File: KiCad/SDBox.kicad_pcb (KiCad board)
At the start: 4 copper layers, 52.5 x 59 mm, 20 parts, among them J1 DB25_Male, J2 Micro_SD_Card_Socket, U1 Rapberry_Pi_Pico_2W, U2 SN74CBT16210

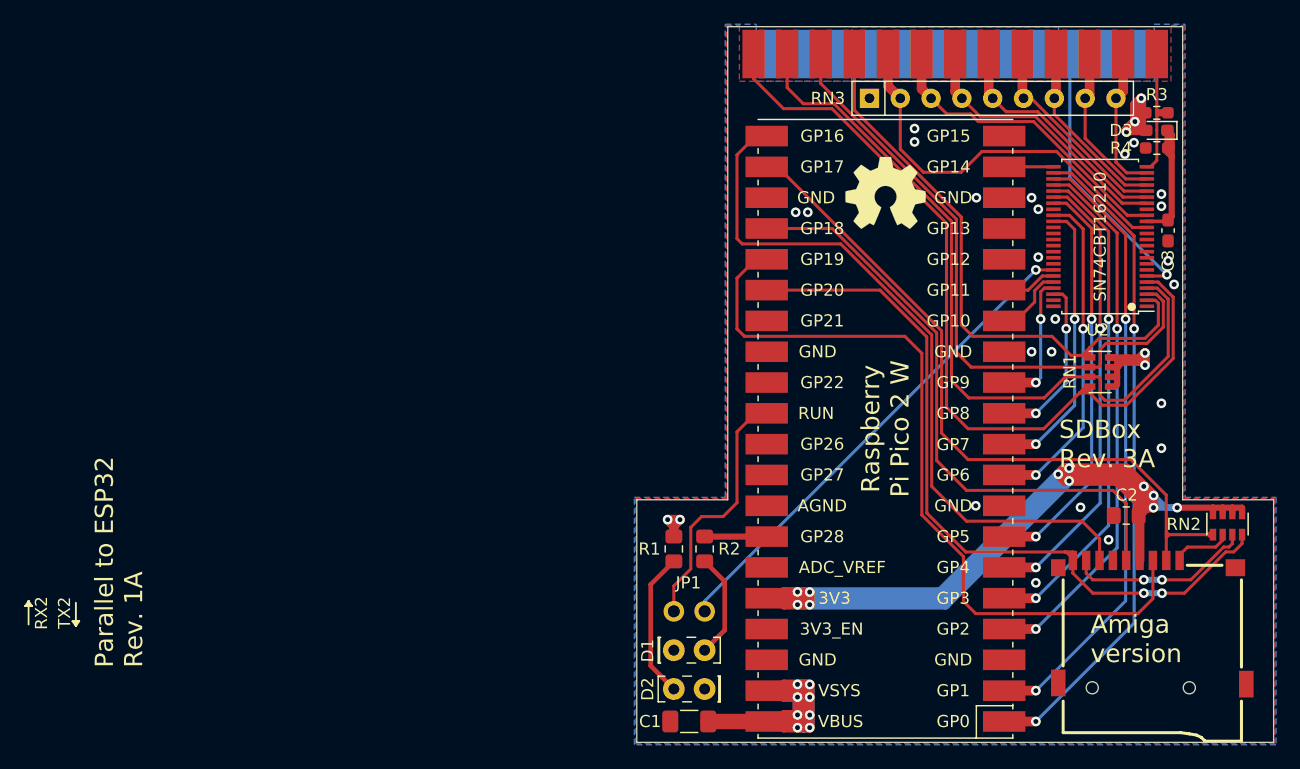
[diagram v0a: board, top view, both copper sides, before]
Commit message: Add UART0_TX and UART0_RX through level shifter
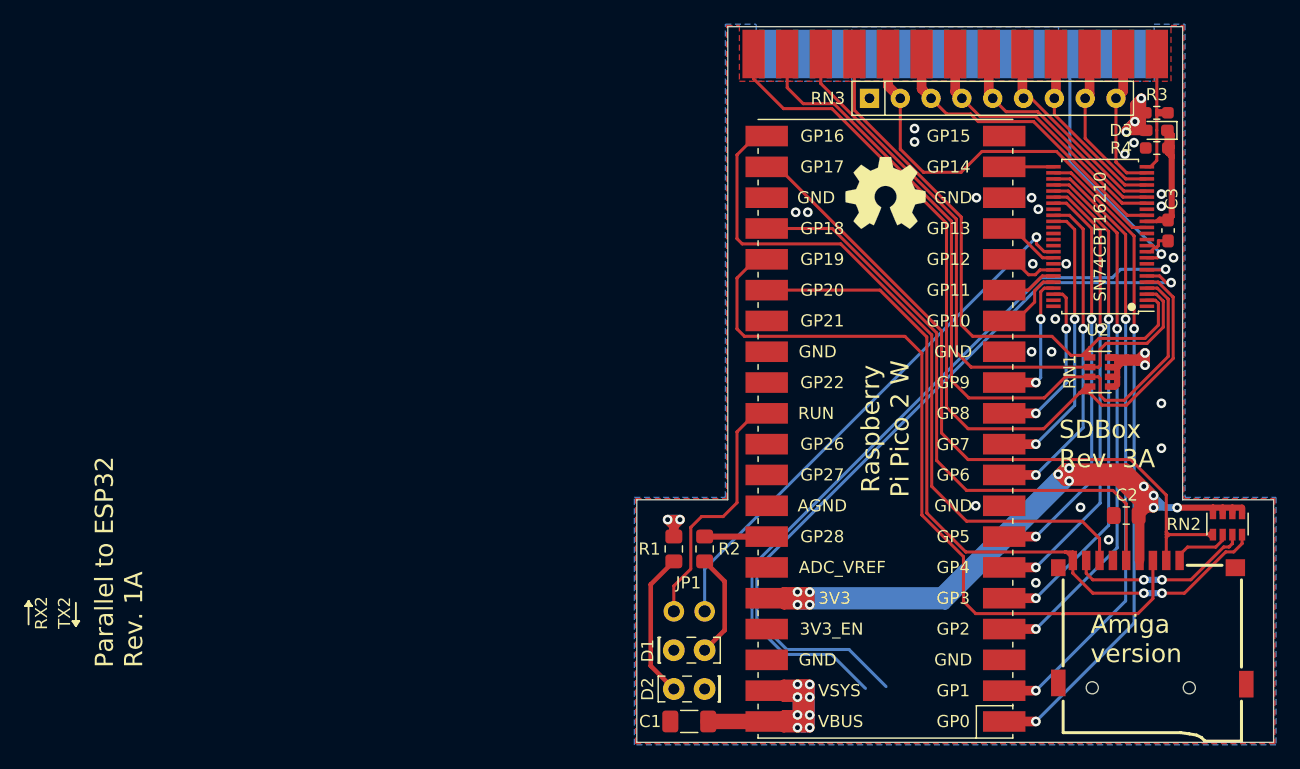
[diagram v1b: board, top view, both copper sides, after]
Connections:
- U1 pad 16: Net-(U1-Pad16) -> UART0_TX_3V3
- U1 pad 17: Net-(U1-Pad17) -> UART0_RX_3V3
- U2 pad 39: Net-(U2-Pad39) -> RESET_3V3
- U2 pad 40: Net-(U2-Pad40) -> UART0_RX_3V3
- U2 pad 42: RESET_3V3 -> UART0_TX_3V3
- U2 pad 6: RESET -> UART0_TX
- U2 pad 7: GND -> UART0_RX
- U2 pad 9: GND -> RESET
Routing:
- net UART0_TX: track 0.00 -> 63.3 mm, vias 0 -> 1
- net UART0_RX: track 0.00 -> 62.0 mm, vias 0 -> 1
- net UART0_RX_3V3: track 0.00 -> 5.96 mm
- net UART0_TX_3V3: track 0.00 -> 5.65 mm
- net RESET_3V3: track 41.0 -> 44.4 mm
- net GND: track 0.00 -> 2.36 mm
- net RESET: track 23.7 -> 21.4 mm
- net VCC: track 75.2 -> 77.2 mm
- net /4V3: track 12.3 -> 13.4 mm

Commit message: Improve ground stitching
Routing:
- net GND: vias 23 -> 33

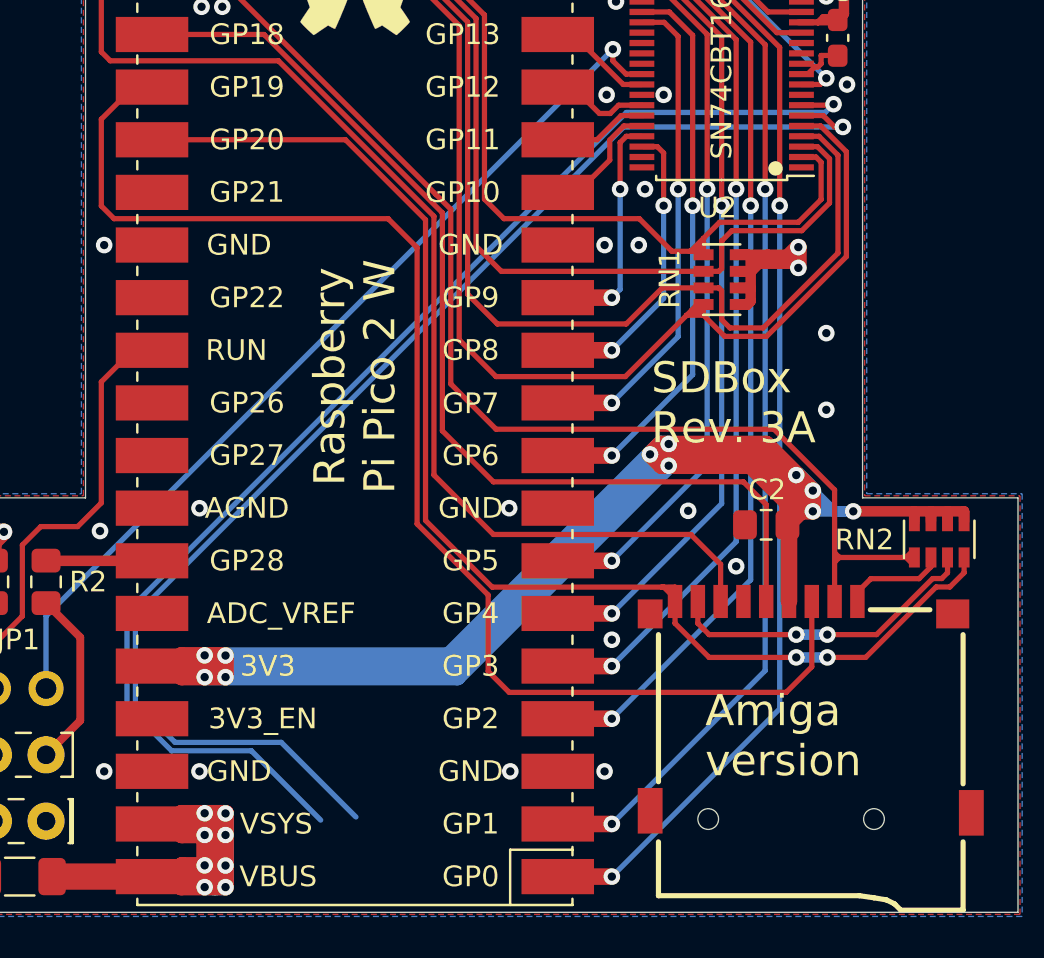
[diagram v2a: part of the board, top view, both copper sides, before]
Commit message: Add UART pinheader on underside with TX0 (GP12), RX0 (GP13) and Power and GND
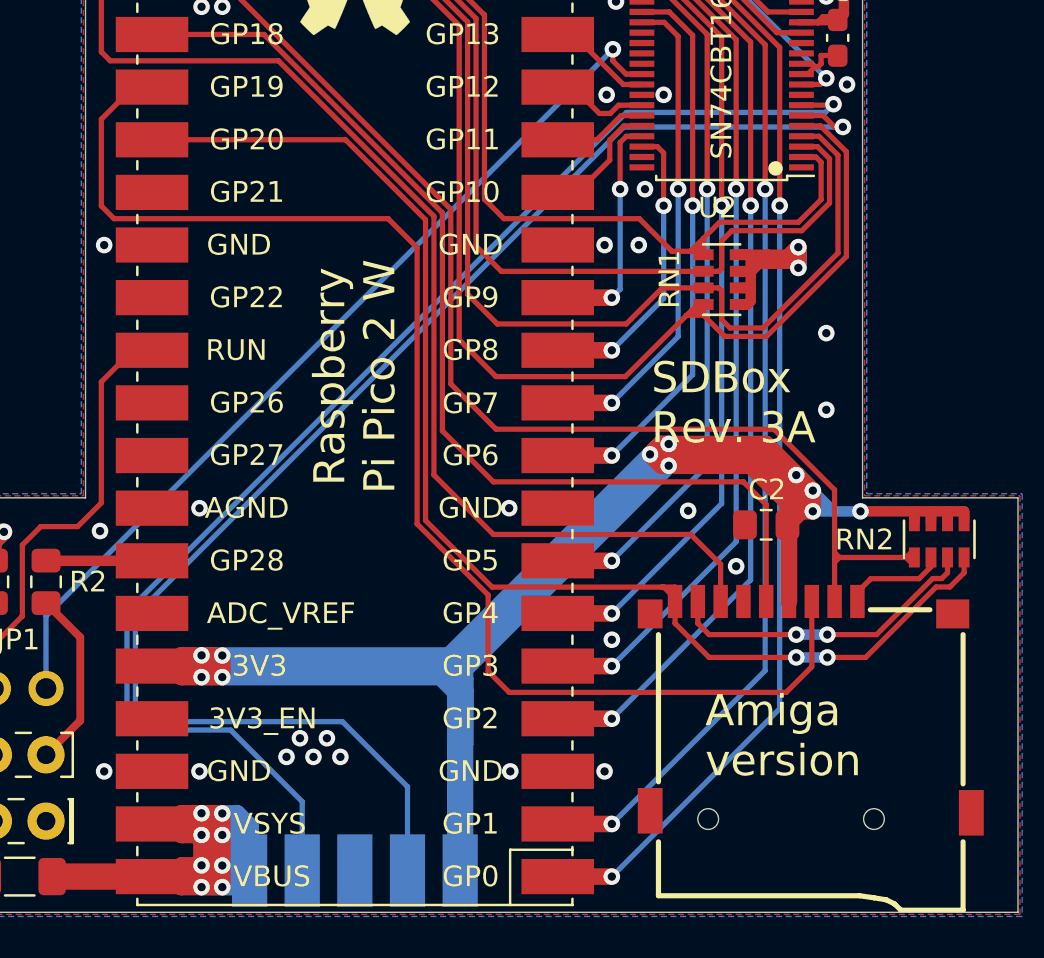
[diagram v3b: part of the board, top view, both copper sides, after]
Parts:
- added J3: Conn_01x05, SDBox:UART_PinHeader_SMD_pads_2.54mm_pitch, B.Cu at (141.9, 142.2)
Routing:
- net 3V3: track 141.7 -> 154.6 mm
- net VCC: track 77.2 -> 88.3 mm
- net UART0_TX: track 63.3 -> 68.3 mm
- net UART0_RX: track 62.0 -> 63.2 mm
- net GND: vias 33 -> 38

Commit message: Improve routing
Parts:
- moved REF** 0.50 mm to (147.7, 113.5)
- moved RN3 0.07 mm to (140.7, 90.9)
- renumbered D2 to D1, D1 to D2
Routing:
- net VCC: track 88.3 -> 86.3 mm
- net CP: track 61.6 -> 60.7 mm
- net UART0_TX: track 68.3 -> 67.6 mm
- net GND: vias 38 -> 41

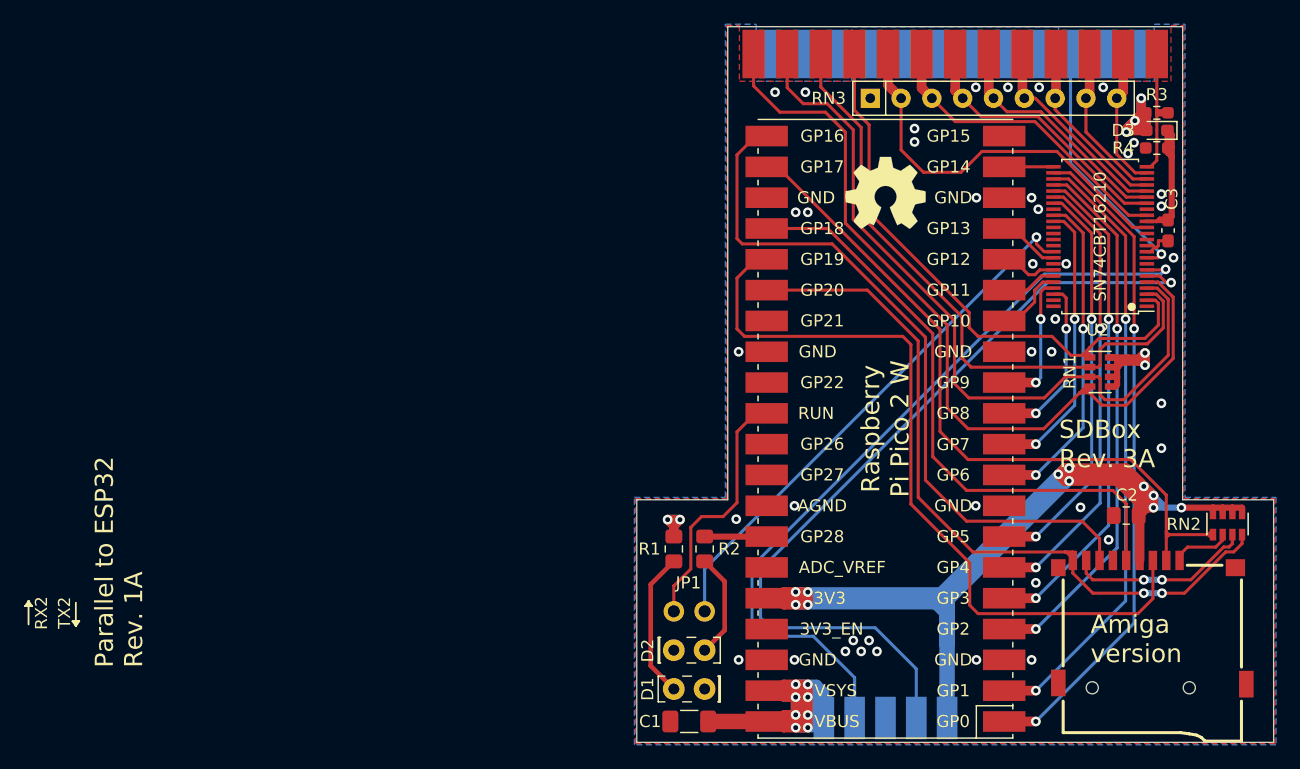
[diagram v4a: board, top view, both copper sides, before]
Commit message: silkscreen fixes
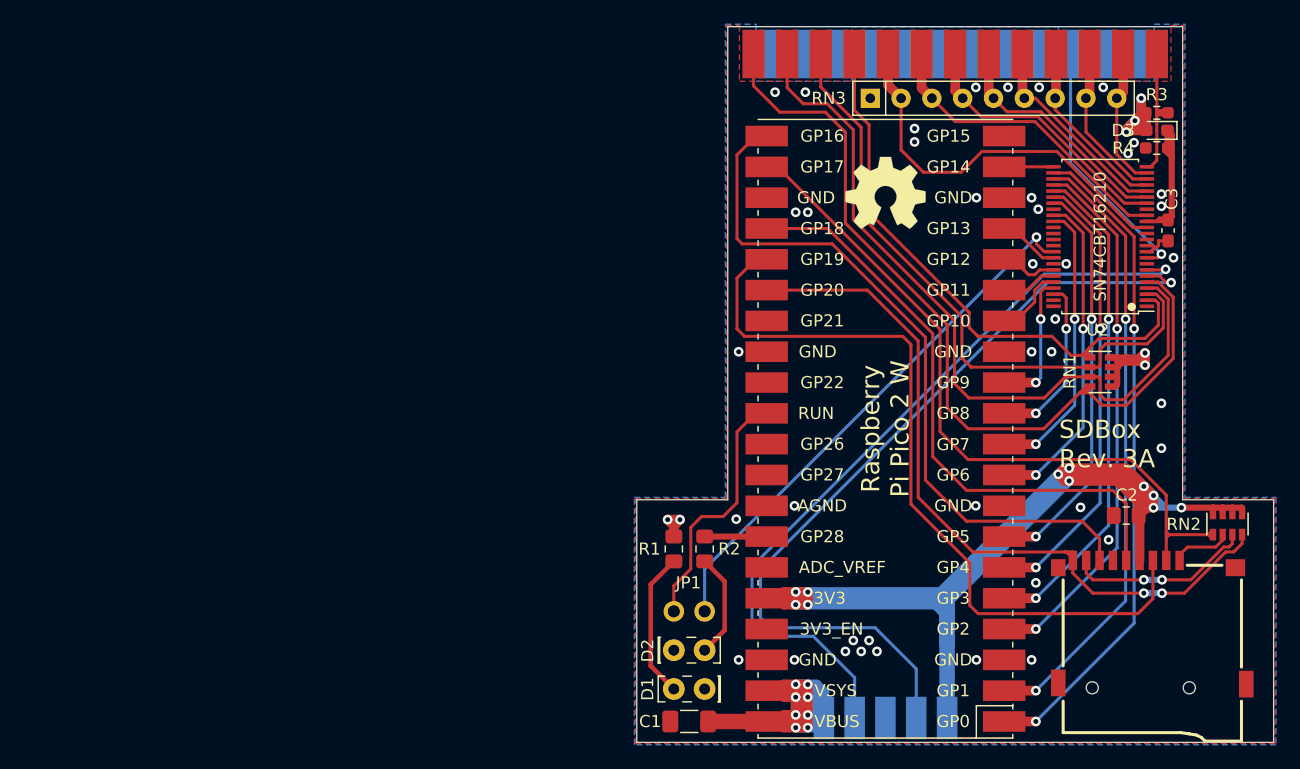
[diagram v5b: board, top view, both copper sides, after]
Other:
- board text added: "(C) 2025 Design by J.Bilander Firmware by N.Ekström"
- board text added: "JLCJLCJLCJLC"
- board text removed: "(C) 2023 Design by J.Bilander"
- board text removed: "Parallel to ESP32 Rev. 1A"
- board text removed: "RX2"
- board text removed: "TX2"
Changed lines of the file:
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@@
   (general
     (thickness 1.6)
-    (drawings 36)
+    (drawings 21)
     (tracks 640)
     (zones 0)
@@
     )
   )
-  (dimension 26.25 (width 0.15) (layer Dwgs.User)
-    (gr_text "26.250 mm" (at 134.575 74.05) (layer Dwgs.User)
-      (effects (font (size 1 1) (thickness 0.15)))
-    )
-    (feature1 (pts (xy 147.7 144) (xy 147.7 74.763579)))
-    (feature2 (pts (xy 121.45 144) (xy 121.45 74.763579)))
-    (crossbar (pts (xy 121.45 75.35) (xy 147.7 75.35)))
-    (arrow1a (pts (xy 147.7 75.35) (xy 146.573496 75.936421)))
-    (arrow1b (pts (xy 147.7 75.35) (xy 146.573496 74.763579)))
-    (arrow2a (pts (xy 121.45 75.35) (xy 122.576504 75.936421)))
-    (arrow2b (pts (xy 121.45 75.35) (xy 122.576504 74.763579)))
-  )
-  (gr_text RX2 (at 72.37 133.34 90) (layer F.SilkS)
-    (effects (font (size 1 1) (thickness 0.15)))
-  )
-  (gr_text TX2 (at 74.27 133.32 90) (layer F.SilkS)
-    (effects (font (size 1 1) (thickness 0.15)))
-  )
-  (gr_line (start 71.31 132.36) (end 71.18 132.76) (layer F.SilkS) (width 0.15))
-  (gr_line (start 71.31 132.36) (end 71.03 132.76) (layer F.SilkS) (width 0.15))
-  (gr_line (start 71.03 132.76) (end 71.59 132.76) (layer F.SilkS) (width 0.15))
-  (gr_line (start 75.21 134.41) (end 75.34 134.01) (layer F.SilkS) (width 0.15))
-  (gr_line (start 75.21 132.49) (end 75.21 134.41) (layer F.SilkS) (width 0.15))
-  (gr_line (start 75.21 134.41) (end 74.93 134.01) (layer F.SilkS) (width 0.15))
-  (gr_line (start 71.31 132.36) (end 71.42 132.76) (layer F.SilkS) (width 0.15))
-  (gr_line (start 75.21 134.41) (end 75.49 134.01) (layer F.SilkS) (width 0.15))
-  (gr_line (start 75.49 134.01) (end 74.93 134.01) (layer F.SilkS) (width 0.15))
-  (gr_line (start 75.21 134.41) (end 75.1 134.01) (layer F.SilkS) (width 0.15))
-  (gr_line (start 71.31 134.28) (end 71.31 132.36) (layer F.SilkS) (width 0.15))
-  (gr_line (start 71.31 132.36) (end 71.59 132.76) (layer F.SilkS) (width 0.15))
+  (gr_text JLCJLCJLCJLC (at 171.45 140 -90) (layer B.SilkS)
+    (effects (font (size 1.2 1.2) (thickness 0.15)) (justify left mirror))
+  )
   (gr_text SN74CBT16210 (at 159.65 102.3 90) (layer F.SilkS)
     (effects (font (size 1 1) (thickness 0.15)))
@@
   (gr_line (start 173.95 124) (end 173.95 144) (layer Edge.Cuts) (width 0.05))
   (gr_line (start 166.45 124) (end 173.95 124) (layer Edge.Cuts) (width 0.05))
-  (gr_text "Amiga\nversion" (at 158.8585 135.4825) (layer F.SilkS)
-    (effects (font (size 1.5 1.5) (thickness 0.2)) (justify left))
+  (gr_text "Amiga\nversion" (at 147.7 99) (layer B.SilkS)
+    (effects (font (size 1.5 1.5) (thickness 0.2)) (justify mirror))
   )
   (gr_text - (at 128.823 139.483) (layer B.SilkS)
@@
     (effects (font (size 1.5 1.5) (thickness 0.2)))
   )
-  (gr_text "(C) 2023\nDesign by J.Bilander" (at 79.3 138.5 270) (layer B.SilkS)
+  (gr_text "(C) 2025\nDesign by J.Bilander\nFirmware by N.Ekström" (at 133.45 124.25 -90) (layer B.SilkS)
     (effects (font (size 1.5 1.5) (thickness 0.2)) (justify left mirror))
-  )
-  (gr_text "Parallel to ESP32\nRev. 1A" (at 78.775 137.84 90) (layer F.SilkS)
-    (effects (font (size 1.5 1.5) (thickness 0.2)) (justify left))
   )
   (gr_line (start 128.95 85) (end 128.95 124) (layer Edge.Cuts) (width 0.05))
@@
   (segment (start 154.4 102.912625) (end 155.037375 103.55) (width 0.254) (layer F.Cu) (net 40))
   (segment (start 154.4 102.35) (end 154.4 102.912625) (width 0.254) (layer F.Cu) (net 40))
+  (segment (start 127.045 136.4) (end 128.696 134.749) (width 0.381) (layer F.Cu) (net 41))
+  (segment (start 128.696 130.729) (end 127.045 129.078) (width 0.381) (layer F.Cu) (net 41))
+  (segment (start 128.696 134.749) (end 128.696 130.729) (width 0.381) (layer F.Cu) (net 41))
   (segment (start 124.505 139.6) (end 122.6 137.695) (width 0.381) (layer F.Cu) (net 42))
   (segment (start 122.6 130.983) (end 124.505 129.078) (width 0.381) (layer F.Cu) (net 42))
   (segment (start 122.6 137.695) (end 122.6 130.983) (width 0.381) (layer F.Cu) (net 42))
-  (segment (start 127.045 136.4) (end 128.696 134.749) (width 0.381) (layer F.Cu) (net 41))
-  (segment (start 128.696 130.729) (end 127.045 129.078) (width 0.381) (layer F.Cu) (net 41))
-  (segment (start 128.696 134.749) (end 128.696 130.729) (width 0.381) (layer F.Cu) (net 41))
   (segment (start 157.4 128.307) (end 157.4 129) (width 0.254) (layer F.Cu) (net 43))
   (segment (start 156.763 128.307) (end 157.4 128.307) (width 0.254) (layer F.Cu) (net 43))
@@
   (segment (start 161.883 112.267) (end 162.983 112.267) (width 0.508) (layer F.Cu) (net 50))
   (segment (start 160.525 112.267) (end 161.883 112.267) (width 0.508) (layer F.Cu) (net 50))
-  (segment (start 163.15 112.7) (end 163.35 112.9) (width 0.508) (layer F.Cu) (net 50))
   (segment (start 161.083 113.067) (end 161.45 112.7) (width 0.508) (layer F.Cu) (net 50))
   (segment (start 161.45 112.7) (end 161.883 112.267) (width 0.508) (layer F.Cu) (net 50))
@@
   (segment (start 161.8176 93.4485) (end 162.5161 92.75) (width 0.8) (layer B.Cu) (net 50))
   (segment (start 161.8176 93.6868) (end 161.8176 93.4485) (width 0.8) (layer B.Cu) (net 50))
+  (segment (start 163.35 112.9) (end 163.15 112.7) (width 0.8) (layer F.Cu) (net 50))
   (segment (start 125.902 126.275) (end 125.902 129.704) (width 0.254) (layer F.Cu) (net 53))
   (segment (start 129.712 124.243) (end 128.569 125.386) (width 0.254) (layer F.Cu) (net 53))
